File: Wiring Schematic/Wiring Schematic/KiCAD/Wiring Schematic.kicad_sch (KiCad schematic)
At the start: 11 parts

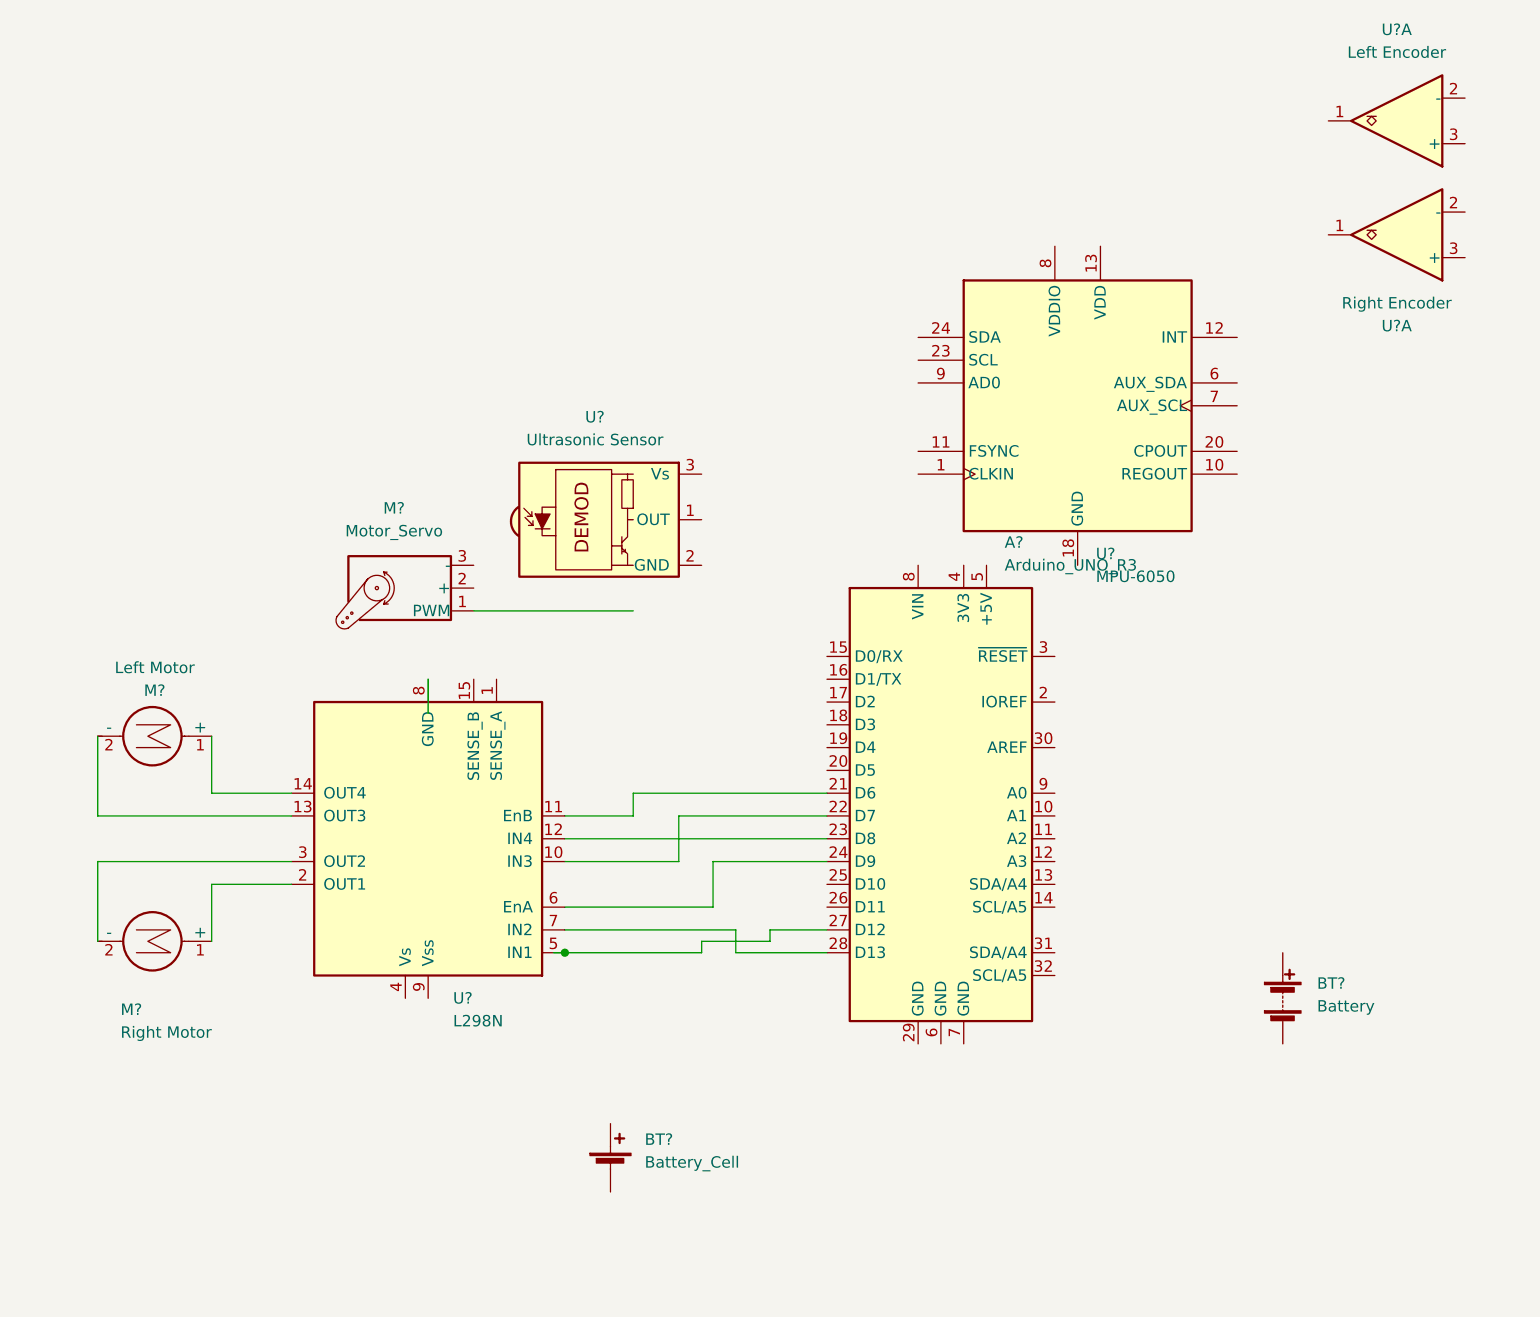
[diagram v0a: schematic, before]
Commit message: Schematic and Task 1 Update
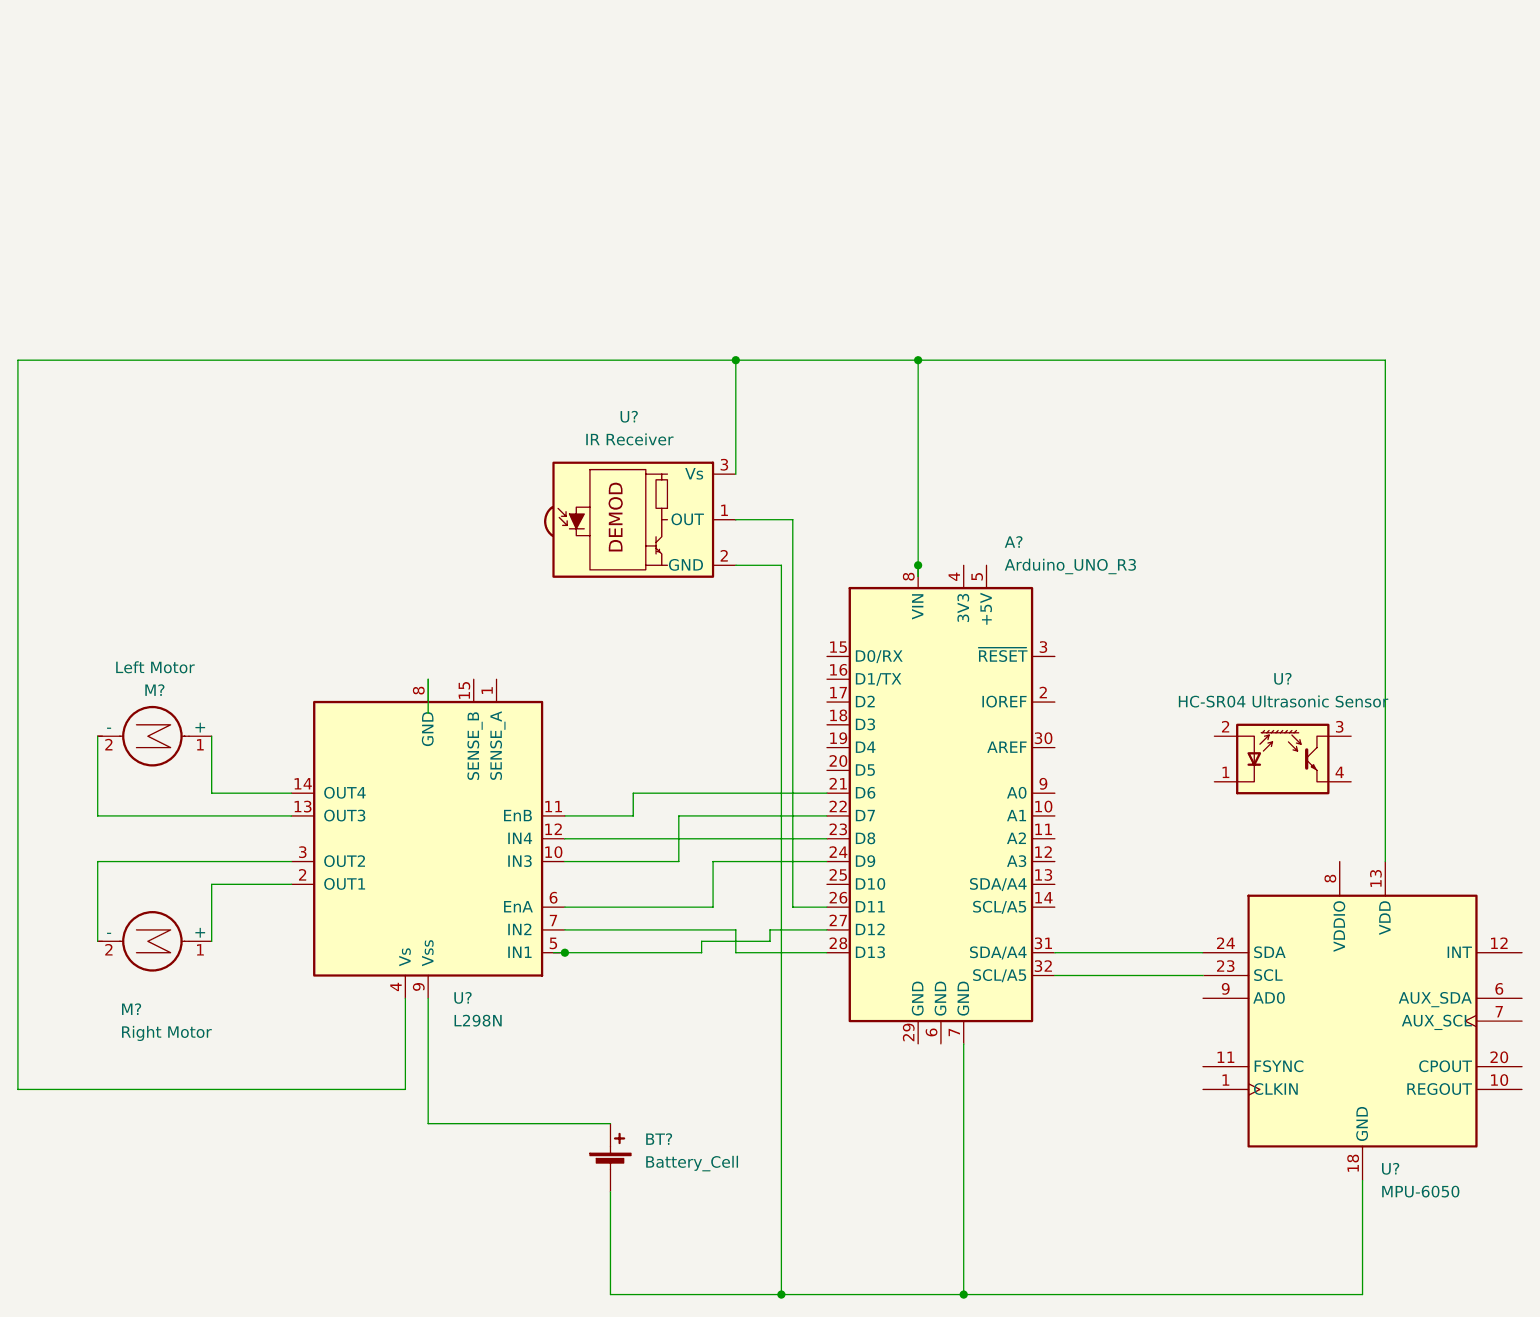
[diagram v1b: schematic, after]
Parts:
- removed BT?: Battery, symbol Device:Battery
- removed M?: Motor_Servo, symbol Motor:Motor_Servo
- removed U?: Left Encoder, symbol Comparator:LM393
- removed U?: Right Encoder, symbol Comparator:LM393
- added U?: HC-SR04 Ultrasonic Sensor, OptoDevice:Everlight_ITR8307, symbol Sensor_Proximity:BPR-105
- U?: value Ultrasonic Sensor -> IR Receiver
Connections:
- net at U?.4 (Vs): now also A?.8 (VIN), U?.13 (VDD), U?.3 (Vs)
- net at U?.9 (Vss): now also BT?.1 (+)
- net at A?.26 (D11): now also U?.1 (OUT)
- net at A?.31 (SDA/A4): now also U?.24 (SDA)
- net at A?.32 (SCL/A5): now also U?.23 (SCL)
- net at A?.7 (GND): now also BT?.2 (-), U?.18 (GND), U?.2 (GND)
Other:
- moved on the sheet: U?
